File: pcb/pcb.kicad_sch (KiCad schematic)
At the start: 14 parts, among them J1 Raspberry_Pi_2_3, SW1 SW_GPIO26, SW2 SW_GPIO19, SW3 SW_GPIO22, SW4 SW_GPIO27, SW5 SW_GPIO17

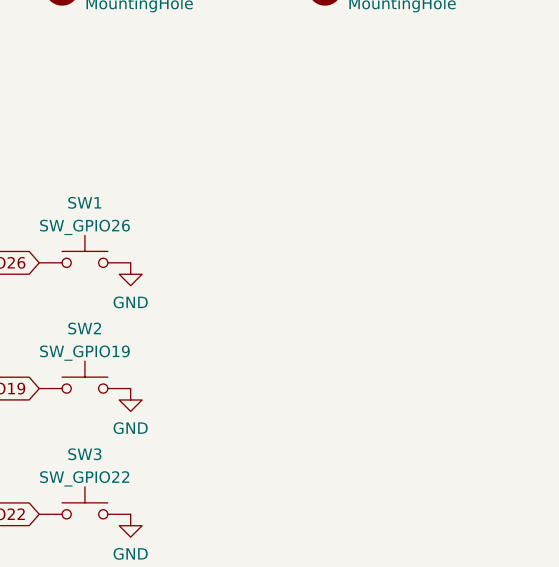
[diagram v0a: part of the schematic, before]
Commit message: add additional pinheader as alternative to button switches
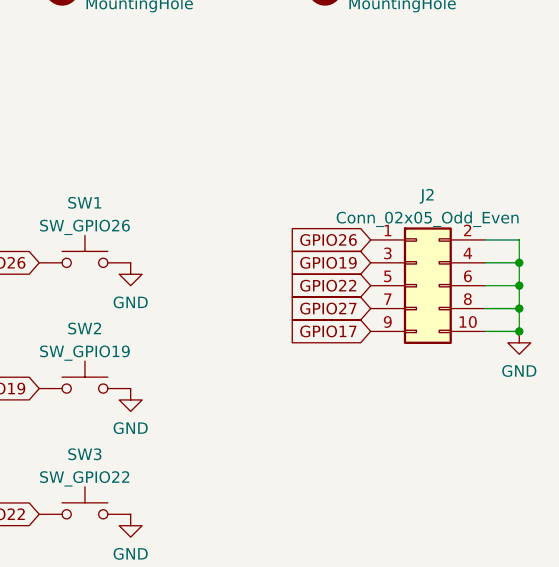
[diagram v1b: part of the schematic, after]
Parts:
- added J2: Conn_02x05_Odd_Even, Connector_PinHeader_2.54mm:PinHeader_2x05_P2.54mm_Vertical, symbol Connector_Generic:Conn_02x05_Odd_Even
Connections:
- net GND: now also J2.10 (Pin_10), J2.2 (Pin_2), J2.4 (Pin_4), J2.6 (Pin_6), J2.8 (Pin_8)
- net GPIO17: now also J2.9 (Pin_9)
- net GPIO19: now also J2.3 (Pin_3)
- net GPIO22: now also J2.5 (Pin_5)
- net GPIO26: now also J2.1 (Pin_1)
- net GPIO27: now also J2.7 (Pin_7)
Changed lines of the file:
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@@
   (junction (at 97.79 107.95) (diameter 0) (color 0 0 0 0)
   )
+  (junction (at 222.25 91.44) (diameter 0) (color 0 0 0 0)
+  )
   (junction (at 100.33 107.95) (diameter 0) (color 0 0 0 0)
   )
   (junction (at 90.17 107.95) (diameter 0) (color 0 0 0 0)
   )
+  (junction (at 222.25 88.9) (diameter 0) (color 0 0 0 0)
+  )
   (junction (at 95.25 107.95) (diameter 0) (color 0 0 0 0)
   )
+  (junction (at 222.25 93.98) (diameter 0) (color 0 0 0 0)
+  )
+  (junction (at 222.25 96.52) (diameter 0) (color 0 0 0 0)
+  )
   (wire (pts (xy 85.09 105.41) (xy 85.09 107.95))
     (stroke (width 0) (type default) (color 0 0 0 0))
   )
+  (wire (pts (xy 218.44 86.36) (xy 222.25 86.36))
+    (stroke (width 0) (type default) (color 0 0 0 0))
+  )
   (wire (pts (xy 97.79 105.41) (xy 97.79 107.95))
     (stroke (width 0) (type default) (color 0 0 0 0))
@@
     (stroke (width 0) (type default) (color 0 0 0 0))
   )
+  (wire (pts (xy 218.44 96.52) (xy 222.25 96.52))
+    (stroke (width 0) (type default) (color 0 0 0 0))
+  )
   (wire (pts (xy 95.25 105.41) (xy 95.25 107.95))
     (stroke (width 0) (type default) (color 0 0 0 0))
@@
     (stroke (width 0) (type default) (color 0 0 0 0))
   )
+  (wire (pts (xy 222.25 91.44) (xy 222.25 93.98))
+    (stroke (width 0) (type default) (color 0 0 0 0))
+  )
+  (wire (pts (xy 222.25 86.36) (xy 222.25 88.9))
+    (stroke (width 0) (type default) (color 0 0 0 0))
+  )
+  (wire (pts (xy 222.25 88.9) (xy 222.25 91.44))
+    (stroke (width 0) (type default) (color 0 0 0 0))
+  )
   (wire (pts (xy 93.98 107.95) (xy 93.98 109.22))
     (stroke (width 0) (type default) (color 0 0 0 0))
   )
+  (wire (pts (xy 218.44 88.9) (xy 222.25 88.9))
+    (stroke (width 0) (type default) (color 0 0 0 0))
+  )
   (wire (pts (xy 90.17 107.95) (xy 92.71 107.95))
     (stroke (width 0) (type default) (color 0 0 0 0))
@@
     (stroke (width 0) (type default) (color 0 0 0 0))
   )
+  (wire (pts (xy 218.44 93.98) (xy 222.25 93.98))
+    (stroke (width 0) (type default) (color 0 0 0 0))
+  )
   (wire (pts (xy 87.63 105.41) (xy 87.63 107.95))
     (stroke (width 0) (type default) (color 0 0 0 0))
@@
     (stroke (width 0) (type default) (color 0 0 0 0))
   )
+  (wire (pts (xy 218.44 91.44) (xy 222.25 91.44))
+    (stroke (width 0) (type default) (color 0 0 0 0))
+  )
+  (wire (pts (xy 222.25 93.98) (xy 222.25 96.52))
+    (stroke (width 0) (type default) (color 0 0 0 0))
+  )
   (wire (pts (xy 92.71 105.41) (xy 92.71 107.95))
     (stroke (width 0) (type default) (color 0 0 0 0))
@@
     )
   )
+  (global_label "GPIO22" (shape input) (at 205.74 91.44 180) (fields_autoplaced)
+    (effects (font (size 1.27 1.27)) (justify right))
+    (property "Referenzen zwischen Schaltplänen" "${INTERSHEET_REFS}" (id 0) (at 196.4326 91.3606 0)
+      (effects (font (size 1.27 1.27)) (justify right) hide)
+    )
+  )
+  (global_label "GPIO26" (shape input) (at 205.74 86.36 180) (fields_autoplaced)
+    (effects (font (size 1.27 1.27)) (justify right))
+    (property "Referenzen zwischen Schaltplänen" "${INTERSHEET_REFS}" (id 0) (at 196.4326 86.2806 0)
+      (effects (font (size 1.27 1.27)) (justify right) hide)
+    )
+  )
   (global_label "GPIO11" (shape input) (at 115.57 85.09 0) (fields_autoplaced)
     (effects (font (size 1.27 1.27)) (justify left))
@@
     )
   )
+  (global_label "GPIO17" (shape input) (at 205.74 96.52 180) (fields_autoplaced)
+    (effects (font (size 1.27 1.27)) (justify right))
+    (property "Referenzen zwischen Schaltplänen" "${INTERSHEET_REFS}" (id 0) (at 196.4326 96.4406 0)
+      (effects (font (size 1.27 1.27)) (justify right) hide)
+    )
+  )
   (global_label "3v3" (shape input) (at 97.79 39.37 90) (fields_autoplaced)
     (effects (font (size 1.27 1.27)) (justify left))
@@
     )
   )
+  (global_label "GPIO19" (shape input) (at 205.74 88.9 180) (fields_autoplaced)
+    (effects (font (size 1.27 1.27)) (justify right))
+    (property "Referenzen zwischen Schaltplänen" "${INTERSHEET_REFS}" (id 0) (at 196.4326 88.8206 0)
+      (effects (font (size 1.27 1.27)) (justify right) hide)
+    )
+  )
   (global_label "GPIO00" (shape input) (at 115.57 49.53 0) (fields_autoplaced)
     (effects (font (size 1.27 1.27)) (justify left))
@@
     (effects (font (size 1.27 1.27)) (justify right))
     (property "Referenzen zwischen Schaltplänen" "${INTERSHEET_REFS}" (id 0) (at 65.6226 79.9306 0)
+      (effects (font (size 1.27 1.27)) (justify right) hide)
+    )
+  )
+  (global_label "GPIO27" (shape input) (at 205.74 93.98 180) (fields_autoplaced)
+    (effects (font (size 1.27 1.27)) (justify right))
+    (property "Referenzen zwischen Schaltplänen" "${INTERSHEET_REFS}" (id 0) (at 196.4326 93.9006 0)
       (effects (font (size 1.27 1.27)) (justify right) hide)
     )
@@
     (pin "2")
   )
+  (symbol (lib_id "power:GND") (at 222.25 96.52 0) (unit 1)
+    (in_bom yes) (on_board yes) (fields_autoplaced)
+    (property "Reference" "#PWR0107" (id 0) (at 222.25 102.87 0)
+      (effects (font (size 1.27 1.27)) hide)
+    )
+    (property "Value" "GND" (id 1) (at 222.25 100.9634 0))
+    (property "Footprint" "" (id 2) (at 222.25 96.52 0)
+      (effects (font (size 1.27 1.27)) hide)
+    )
+    (property "Datasheet" "" (id 3) (at 222.25 96.52 0)
+      (effects (font (size 1.27 1.27)) hide)
+    )
+    (pin "1")
+  )
   (symbol (lib_id "power:GND") (at 179.07 146.05 0) (unit 1)
     (in_bom yes) (on_board yes) (fields_autoplaced)
@@
     )
   )
+  (symbol (lib_id "Connector_Generic:Conn_02x05_Odd_Even") (at 210.82 91.44 0) (unit 1)
+    (in_bom yes) (on_board yes) (fields_autoplaced)
+    (property "Reference" "J2" (id 0) (at 212.09 81.3902 0))
+    (property "Value" "Conn_02x05_Odd_Even" (id 1) (at 212.09 83.9271 0))
+    (property "Footprint" "Connector_PinHeader_2.54mm:PinHeader_2x05_P2.54mm_Vertical" (id 2) (at 210.82 91.44 0)
+      (effects (font (size 1.27 1.27)) hide)
+    )
+    (property "Datasheet" "~" (id 3) (at 210.82 91.44 0)
+      (effects (font (size 1.27 1.27)) hide)
+    )
+    (pin "1")
+    (pin "10")
+    (pin "2")
+    (pin "3")
+    (pin "4")
+    (pin "5")
+    (pin "6")
+    (pin "7")
+    (pin "8")
+    (pin "9")
+  )
   (symbol (lib_id "power:GND") (at 179.07 130.81 0) (unit 1)
     (in_bom yes) (on_board yes) (fields_autoplaced)
@@
       (reference "#PWR0106") (unit 1) (value "GND") (footprint "")
     )
+    (path "/20c37316-d6de-43a0-b667-bb1633c68dc7"
+      (reference "#PWR0107") (unit 1) (value "GND") (footprint "")
+    )
     (path "/e0fbf76e-88c0-4895-9f77-371ffe7e4c9e"
       (reference "H1") (unit 1) (value "MountingHole") (footprint "MountingHole:MountingHole_2.7mm_M2.5_Pad_Via")
@@
       (reference "J1") (unit 1) (value "Raspberry_Pi_2_3") (footprint "Connector_PinSocket_2.54mm:PinSocket_2x20_P2.54mm_Vertical")
     )
+    (path "/9b66f880-6330-4109-b0bd-72043ab64f13"
+      (reference "J2") (unit 1) (value "Conn_02x05_Odd_Even") (footprint "Connector_PinHeader_2.54mm:PinHeader_2x05_P2.54mm_Vertical")
+    )
     (path "/565e1796-a517-4e0e-b459-c778804203ee"
